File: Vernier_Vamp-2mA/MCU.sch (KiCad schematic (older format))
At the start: 11 parts

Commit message: 1.0C Initial commit
-Fixed amplifier output
-Changed connectors to IDC
-Via perimeter added
TODO:
Add shielding over analogue section
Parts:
- removed A1: Arduino_Nano_v3.x, Module:Arduino_Nano, symbol MCU_Module:Arduino_Nano_v3.x
- removed R50: 0R, Resistor_SMD:R_0603_1608Metric_Pad1.05x0.95mm_HandSolder, symbol Device:R_Small
- added A1: Arduino_Nano_Every, Module:Arduino_Nano, symbol MCU_Module:Arduino_Nano_Every
- added JP3, JP4: SolderJumper_2_Open, Jumper:SolderJumper-2_P1.3mm_Open_Pad1.0x1.5mm, symbol Jumper:SolderJumper_2_Open
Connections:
- net labels added: +5V
- no-connect marks 20 -> 19
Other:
- note added: "MPM3610 SMPS\n(Potentially noisy)"
- note added: "Schottky diode on the USB 5V rail.\nDon't bridge if Vin is used."
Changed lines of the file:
@@
 Comment4 ""
 $EndDescr
-$Comp
-L power:GNDD #PWR0196
-U 1 1 5E449396
-P 5900 5050
-AR Path="/5E1DEB8C/5E449396" Ref="#PWR0196"  Part="1"
-AR Path="/5E5EF2D7/5E449396" Ref="#PWR?"  Part="1"
-F 0 "#PWR0196" H 5900 4800 50  0001 C CNN
-F 1 "GNDD" H 5904 4895 50  0000 C CNN
-F 2 "" H 5900 5050 50  0001 C CNN
-F 3 "" H 5900 5050 50  0001 C CNN
-	1    5900 5050
-	1    0    0    -1
-$EndComp
-Wire Wire Line
-	5850 4800 5850 4900
-Wire Wire Line
-	5850 4900 5900 4900
-Wire Wire Line
-	5950 4900 5950 4800
-Wire Wire Line
-	5900 4900 5900 5050
-Connection ~ 5900 4900
-Wire Wire Line
-	5900 4900 5950 4900
 Text HLabel 4700 4500 0    50   Output ~ 0
 CLK
-Text HLabel 4700 4200 0    50   Output ~ 0
+Text HLabel 4700 4100 0    50   Output ~ 0
 ~CS
+Text HLabel 4700 4300 0    50   Output ~ 0
+SDI
+Text HLabel 4700 4400 0    50   Output ~ 0
+SDO
 Wire Wire Line
 	5350 4500 4700 4500
 Wire Wire Line
-	4700 4200 5350 4200
+	4700 4100 5350 4100
+Wire Wire Line
+	4700 4300 5350 4300
 Wire Wire Line
 	4700 4400 5350 4400
-Wire Wire Line
-	4700 4300 5350 4300
-NoConn ~ 5350 3700
-NoConn ~ 5350 3600
-NoConn ~ 5350 3500
-NoConn ~ 5350 3400
-NoConn ~ 6350 3600
-NoConn ~ 6350 3800
-NoConn ~ 6350 3900
-NoConn ~ 6350 4000
-NoConn ~ 6350 4100
-NoConn ~ 6350 4200
-NoConn ~ 6350 4300
-NoConn ~ 6350 4400
-NoConn ~ 6350 4500
-Text HLabel 4700 4100 0    50   Output ~ 0
+Text HLabel 4700 4000 0    50   Output ~ 0
 ~LDAC
-Text HLabel 4700 4000 0    50   Output ~ 0
+Text HLabel 4700 3900 0    50   Output ~ 0
 MSB
-NoConn ~ 5350 3800
-Wire Wire Line
-	4700 4000 5350 4000
-Wire Wire Line
-	5350 4100 4700 4100
+Wire Wire Line
+	4700 3900 5350 3900
+Wire Wire Line
+	5350 4000 4700 4000
 Text HLabel 4150 5900 2    50   Output ~ 0
 ~RS
-NoConn ~ 5350 3200
-NoConn ~ 5350 3300
-NoConn ~ 5950 2800
 $Comp
 L power:GNDD #PWR0205
@@
 	2350 6200 2350 6750
 $Comp
-L MCU_Module:Arduino_Nano_v3.x A1
-U 1 1 5E447129
-P 5850 3800
-AR Path="/5E1DEB8C/5E447129" Ref="A1"  Part="1"
-AR Path="/5E5EF2D7/5E447129" Ref="A?"  Part="1"
-F 0 "A1" H 6350 5050 50  0000 C CNN
-F 1 "Arduino_Nano_v3.x" H 6450 4950 50  0000 C CNN
-F 2 "Module:Arduino_Nano" H 5850 3800 50  0001 C CIN
-F 3 "http://www.mouser.com/pdfdocs/Gravitech_Arduino_Nano3_0.pdf" H 5850 3800 50  0001 C CNN
-	1    5850 3800
-	1    0    0    -1
-$EndComp
-$Comp
 L power:+5VD #PWR0117
 U 1 1 610CFB70
@@
 Text HLabel 4150 6500 2    50   Output ~ 0
 ~CS
+Text HLabel 4150 6350 2    50   Output ~ 0
+SDI
 Text HLabel 4150 6200 2    50   Output ~ 0
-SDI
+SDO
 Wire Wire Line
 	3500 6050 4150 6050
@@
 	4150 6500 3500 6500
 Wire Wire Line
+	4150 6350 3500 6350
+Wire Wire Line
 	4150 6200 3500 6200
-Wire Wire Line
-	4150 6350 3500 6350
 Text HLabel 4150 6650 2    50   Output ~ 0
 ~LDAC
@@
 Wire Wire Line
 	4150 5900 3500 5900
-Text HLabel 4700 3900 0    50   Output ~ 0
+Text HLabel 4700 3800 0    50   Output ~ 0
 ~RS
 Wire Wire Line
-	5350 3900 4700 3900
-NoConn ~ 6350 3200
-NoConn ~ 6350 3300
-NoConn ~ 8000 4750
-Wire Wire Line
-	6050 2550 6050 2800
+	5350 3800 4700 3800
+Wire Wire Line
+	6050 2550 6050 2650
 Wire Wire Line
 	5750 2650 5750 2800
 Wire Wire Line
 	4700 2650 4700 2550
-Wire Wire Line
-	4700 2650 5100 2650
-$Comp
-L Device:R_Small R?
-U 1 1 5EE38105
-P 5200 2650
-AR Path="/5E1DD6A9/5EE38105" Ref="R?"  Part="1"
-AR Path="/5E1DD6A9/5EC279B2/5EE38105" Ref="R?"  Part="1"
-AR Path="/5E1DEB8C/5EE38105" Ref="R50"  Part="1"
-F 0 "R50" V 5004 2650 50  0000 C CNN
-F 1 "0R" V 5095 2650 50  0000 C CNN
-F 2 "Resistor_SMD:R_0603_1608Metric_Pad1.05x0.95mm_HandSolder" H 5200 2650 50  0001 C CNN
-F 3 "~" H 5200 2650 50  0001 C CNN
-	1    5200 2650
-	0    1    1    0
-$EndComp
 $Comp
 L power:PWR_FLAG #FLG0107
@@
 Wire Wire Line
 	5450 2650 5750 2650
-Text HLabel 4150 6350 2    50   Output ~ 0
-SDO
 Text HLabel 4700 4400 0    50   Output ~ 0
 SDO
 Text HLabel 4700 4300 0    50   Output ~ 0
 SDI
+NoConn ~ 5350 3000
+NoConn ~ 5350 3100
+NoConn ~ 5350 3300
+NoConn ~ 5350 3400
+NoConn ~ 5350 3500
+NoConn ~ 5350 3600
+NoConn ~ 5350 3700
+NoConn ~ 6350 3600
+NoConn ~ 6350 3200
+NoConn ~ 6350 3300
+NoConn ~ 6350 3800
+NoConn ~ 6350 3900
+NoConn ~ 6350 4000
+NoConn ~ 6350 4100
+NoConn ~ 6350 4200
+NoConn ~ 6350 4300
+NoConn ~ 6350 4400
+NoConn ~ 6350 4500
+Wire Wire Line
+	5850 4800 5850 4950
+$Comp
+L power:GNDD #PWR0196
+U 1 1 5FA351DD
+P 5850 4950
+AR Path="/5E1DEB8C/5FA351DD" Ref="#PWR0196"  Part="1"
+AR Path="/5E5EF2D7/5FA351DD" Ref="#PWR?"  Part="1"
+F 0 "#PWR0196" H 5850 4700 50  0001 C CNN
+F 1 "GNDD" H 5854 4795 50  0000 C CNN
+F 2 "" H 5850 4950 50  0001 C CNN
+F 3 "" H 5850 4950 50  0001 C CNN
+	1    5850 4950
+	1    0    0    -1
+$EndComp
+$Comp
+L MCU_Module:Arduino_Nano_Every A1
+U 1 1 5FA2A758
+P 5850 3800
+F 0 "A1" H 5250 2850 50  0000 C CNN
+F 1 "Arduino_Nano_Every" H 5000 2750 50  0000 C CNN
+F 2 "Module:Arduino_Nano" H 5850 3800 50  0001 C CIN
+F 3 "https://content.arduino.cc/assets/NANOEveryV3.0_sch.pdf" H 5850 3800 50  0001 C CNN
+	1    5850 3800
+	1    0    0    -1
+$EndComp
+NoConn ~ 5950 2800
+$Comp
+L Jumper:SolderJumper_2_Open JP3
+U 1 1 5FB9E809
+P 5150 2650
+F 0 "JP3" H 5150 2763 50  0000 C CNN
+F 1 "SolderJumper_2_Open" H 5150 2764 50  0001 C CNN
+F 2 "Jumper:SolderJumper-2_P1.3mm_Open_Pad1.0x1.5mm" H 5150 2650 50  0001 C CNN
+F 3 "~" H 5150 2650 50  0001 C CNN
+	1    5150 2650
+	1    0    0    -1
+$EndComp
+Wire Wire Line
+	4700 2650 5000 2650
+$Comp
+L Jumper:SolderJumper_2_Open JP4
+U 1 1 5FBA0FCC
+P 6450 2650
+F 0 "JP4" H 6450 2763 50  0000 C CNN
+F 1 "SolderJumper_2_Open" H 6450 2764 50  0001 C CNN
+F 2 "Jumper:SolderJumper-2_P1.3mm_Open_Pad1.0x1.5mm" H 6450 2650 50  0001 C CNN
+F 3 "~" H 6450 2650 50  0001 C CNN
+	1    6450 2650
+	1    0    0    -1
+$EndComp
+$Comp
+L power:+5V #PWR?
+U 1 1 5FBA78FF
+P 6750 2550
+AR Path="/5E1DD6A9/5FBA78FF" Ref="#PWR?"  Part="1"
+AR Path="/5E1DEB8C/5FBA78FF" Ref="#PWR0212"  Part="1"
+F 0 "#PWR0212" H 6750 2400 50  0001 C CNN
+F 1 "+5V" H 6765 2723 50  0000 C CNN
+F 2 "" H 6750 2550 50  0001 C CNN
+F 3 "" H 6750 2550 50  0001 C CNN
+	1    6750 2550
+	1    0    0    -1
+$EndComp
+Wire Wire Line
+	6300 2650 6050 2650
+Connection ~ 6050 2650
+Wire Wire Line
+	6050 2650 6050 2800
+Wire Wire Line
+	6600 2650 6750 2650
+Wire Wire Line
+	6750 2650 6750 2550
+Text Notes 4500 2950 0    50   ~ 0
+MPM3610 SMPS\n(Potentially noisy)
+Wire Notes Line
+	5300 2500 5300 2750
+Wire Notes Line
+	5300 2750 5000 2750
+Wire Notes Line
+	5000 2750 5000 2500
+Wire Notes Line
+	5000 2500 5300 2500
+Text Notes 6450 2950 0    50   ~ 0
+Schottky diode on the USB 5V rail.\nDon't bridge if Vin is used.
+Wire Notes Line
+	6600 2750 6300 2750
+Wire Notes Line
+	6300 2750 6300 2500
+Wire Notes Line
+	6300 2500 6600 2500
+Wire Notes Line
+	6600 2500 6600 2750
 $EndSCHEMATC

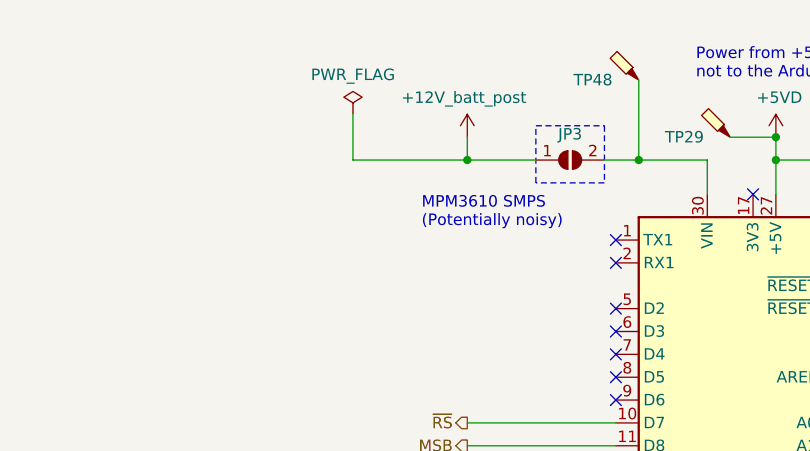
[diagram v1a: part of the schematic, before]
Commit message: Issue fixes
This commit, addresses following issues:
-Stray current at the output with only USB plugged in
-RFI Shield over analogue circuitry
-Wrong BNC connector footprint

Some general layout optimisation
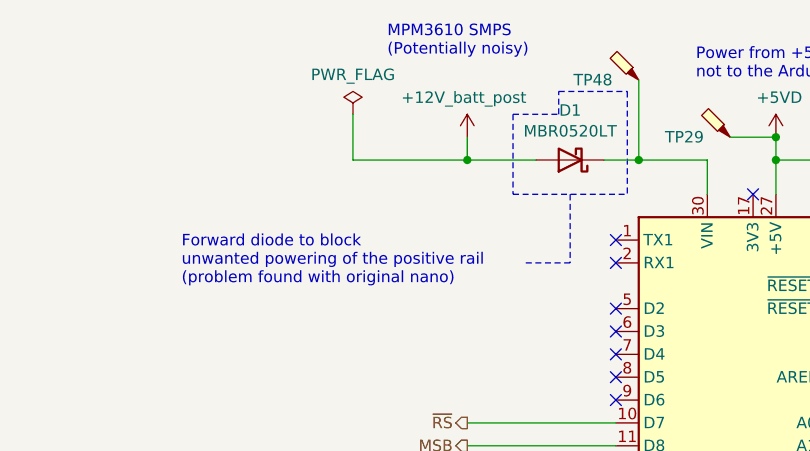
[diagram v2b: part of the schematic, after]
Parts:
- removed JP3: SolderJumper_2_Open, Jumper:SolderJumper-2_P1.3mm_Open_Pad1.0x1.5mm, symbol Jumper:SolderJumper_2_Open
- added D1: MBR0520LT, Diode_SMD:D_SOD-123, symbol Diode:MBR0520LT
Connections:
- net +12V_batt_post: now also D1.2 (A)
- net at A1.30 (VIN), TP48.1: now also D1.1 (K)
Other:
- note added: "Forward diode to block\nunwanted powering of the positive rail\n(problem found with original nano)"
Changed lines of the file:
@@
 $EndComp
 NoConn ~ 5950 2800
-$Comp
-L Jumper:SolderJumper_2_Open JP3
-U 1 1 5FB9E809
-P 5150 2650
-F 0 "JP3" H 5150 2763 50  0000 C CNN
-F 1 "SolderJumper_2_Open" H 5150 2764 50  0001 C CNN
-F 2 "Jumper:SolderJumper-2_P1.3mm_Open_Pad1.0x1.5mm" H 5150 2650 50  0001 C CNN
-F 3 "~" H 5150 2650 50  0001 C CNN
-	1    5150 2650
-	1    0    0    -1
-$EndComp
 Wire Wire Line
 	4700 2650 5000 2650
@@
 Wire Wire Line
 	6750 2650 6750 2550
-Text Notes 4500 2950 0    50   ~ 0
+Text Notes 4350 2200 0    50   ~ 0
 MPM3610 SMPS\n(Potentially noisy)
-Wire Notes Line
-	5300 2500 5300 2750
-Wire Notes Line
-	5300 2750 5000 2750
-Wire Notes Line
-	5000 2750 5000 2500
-Wire Notes Line
-	5000 2500 5300 2500
 Text Notes 6450 2950 0    50   ~ 0
 Schottky diode on the USB 5V rail.\nDon't bridge if Vin is used.
@@
 Wire Notes Line
 	6600 2500 6600 2750
+Wire Notes Line
+	4900 2450 5100 2450
+Wire Notes Line
+	5100 2450 5100 2350
+Wire Notes Line
+	5400 2350 5400 2800
+Wire Notes Line
+	4900 2450 4900 2800
+Wire Notes Line
+	5150 2800 5150 3100
+Wire Notes Line
+	5150 3100 4950 3100
+Text Notes 3450 3200 0    50   ~ 0
+Forward diode to block\nunwanted powering of the positive rail\n(problem found with original nano)
+$Comp
+L Diode:MBR0520LT D1
+U 1 1 5FC37ED8
+P 5150 2650
+F 0 "D1" H 5150 2433 50  0000 C CNN
+F 1 "MBR0520LT" H 5150 2524 50  0000 C CNN
+F 2 "Diode_SMD:D_SOD-123" H 5150 2475 50  0001 C CNN
+F 3 "http://www.onsemi.com/pub_link/Collateral/MBR0520LT1-D.PDF" H 5150 2650 50  0001 C CNN
+	1    5150 2650
+	-1   0    0    1
+$EndComp
+Wire Notes Line
+	5100 2350 5400 2350
+Wire Notes Line
+	4900 2800 5400 2800
 $EndSCHEMATC

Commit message: Change of J1 connector courtyard
PCB footprint change:
-J1 (1 mm pinheader) courtyard had been changed to pass DRC
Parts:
- A1: symbol MCU_Module:Arduino_Nano_Every -> Vernier_Vamp-2mA-rescue:Arduino_Nano_Every-MCU_Module
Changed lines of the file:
@@
 $EndComp
 $Comp
-L MCU_Module:Arduino_Nano_Every A1
+L Vernier_Vamp-2mA-rescue:Arduino_Nano_Every-MCU_Module A1
 U 1 1 5FA2A758
 P 5850 3800
+AR Path="/5FA2A758" Ref="A1"  Part="1"
+AR Path="/5E1DEB8C/5FA2A758" Ref="A1"  Part="1"
 F 0 "A1" H 5250 2850 50  0000 C CNN
 F 1 "Arduino_Nano_Every" H 5000 2750 50  0000 C CNN

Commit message: 1.0D Update
LCCD changes
-Addition of trigger for calibration
-PCB optimisation

HCCD changes
-New output stage designed
-Changes from 1.0C applied to HCCD
-New more optimised layout
-New shielding over analog section
-Addition of trigger for calibration

New symbols and footprint creation
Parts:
- removed JP4: SolderJumper_2_Open, Jumper:SolderJumper-2_P1.3mm_Open_Pad1.0x1.5mm, symbol Jumper:SolderJumper_2_Open
- added D2: MBR0520LT, Diode_SMD:D_SOD-123, symbol Diode:MBR0520LT
- added J9: Conn_01x02, Connector_PinHeader_2.54mm:PinHeader_1x02_P2.54mm_Vertical, symbol Connector_Generic:Conn_01x02
- A1: symbol Vernier_Vamp-2mA-rescue:Arduino_Nano_Every-MCU_Module -> Vernier_Vamp-2mA-rescue:Arduino_Nano_Every-MCU_Module-Vernier_Vamp-2mA-rescue
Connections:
- net +5V: now also D2.2 (A)
- net +5VD: now also D2.1 (K)
- net GNDD: now also J9.2 (Pin_2)
- net Trigger: now reaches A1.19 (A0)
- net Trigger: now also J9.1 (Pin_1)
- no-connect marks 19 -> 18
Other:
- note added: "Trigger output for calibration"
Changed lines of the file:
@@
 encoding utf-8
 Sheet 5 7
-Title "\"Vernier Vamp\" Coil Driver - 2mA"
-Date "2020-05-05"
-Rev "1.0B"
+Title "\"Vernier Vamp\" Coil Driver - LCCD"
+Date "2021-05-18"
+Rev "1.0D"
 Comp "Strathclyde University"
 Comment1 "Designed by: Marcin Mrozowski"
@@
 	4150 6500 3500 6500
 Wire Wire Line
+	4150 6200 3500 6200
+Wire Wire Line
 	4150 6350 3500 6350
-Wire Wire Line
-	4150 6200 3500 6200
 Text HLabel 4150 6650 2    50   Output ~ 0
 ~LDAC
@@
 NoConn ~ 6350 3200
 NoConn ~ 6350 3300
-NoConn ~ 6350 3800
 NoConn ~ 6350 3900
 NoConn ~ 6350 4000
@@
 $EndComp
 $Comp
-L Vernier_Vamp-2mA-rescue:Arduino_Nano_Every-MCU_Module A1
+L Vernier_Vamp-2mA-rescue:Arduino_Nano_Every-MCU_Module-Vernier_Vamp-2mA-rescue A1
 U 1 1 5FA2A758
 P 5850 3800
@@
 Wire Wire Line
 	4700 2650 5000 2650
-$Comp
-L Jumper:SolderJumper_2_Open JP4
-U 1 1 5FBA0FCC
-P 6450 2650
-F 0 "JP4" H 6450 2763 50  0000 C CNN
-F 1 "SolderJumper_2_Open" H 6450 2764 50  0001 C CNN
-F 2 "Jumper:SolderJumper-2_P1.3mm_Open_Pad1.0x1.5mm" H 6450 2650 50  0001 C CNN
-F 3 "~" H 6450 2650 50  0001 C CNN
-	1    6450 2650
-	1    0    0    -1
-$EndComp
 $Comp
 L power:+5V #PWR?
@@
 Wire Notes Line
 	4900 2800 5400 2800
+$Comp
+L Diode:MBR0520LT D2
+U 1 1 609E1E99
+P 6450 2650
+F 0 "D2" H 6450 2900 50  0000 C CNN
+F 1 "MBR0520LT" H 6450 2800 50  0000 C CNN
+F 2 "Diode_SMD:D_SOD-123" H 6450 2475 50  0001 C CNN
+F 3 "http://www.onsemi.com/pub_link/Collateral/MBR0520LT1-D.PDF" H 6450 2650 50  0001 C CNN
+	1    6450 2650
+	1    0    0    -1
+$EndComp
+$Comp
+L Connector_Generic:Conn_01x02 J9
+U 1 1 60A430EA
+P 1400 6100
+F 0 "J9" H 1480 6092 50  0000 L CNN
+F 1 "Conn_01x02" H 1480 6001 50  0000 L CNN
+F 2 "Connector_PinHeader_2.54mm:PinHeader_1x02_P2.54mm_Vertical" H 1400 6100 50  0001 C CNN
+F 3 "~" H 1400 6100 50  0001 C CNN
+	1    1400 6100
+	-1   0    0    -1
+$EndComp
+$Comp
+L power:GNDD #PWR0214
+U 1 1 60A4542E
+P 1600 6300
+AR Path="/5E1DEB8C/60A4542E" Ref="#PWR0214"  Part="1"
+AR Path="/5E5EF2D7/60A4542E" Ref="#PWR?"  Part="1"
+F 0 "#PWR0214" H 1600 6050 50  0001 C CNN
+F 1 "GNDD" H 1604 6145 50  0000 C CNN
+F 2 "" H 1600 6300 50  0001 C CNN
+F 3 "" H 1600 6300 50  0001 C CNN
+	1    1600 6300
+	1    0    0    -1
+$EndComp
+Wire Wire Line
+	1600 6200 1600 6300
+Wire Wire Line
+	6350 3800 7000 3800
+Text Label 7000 3800 0    50   ~ 0
+Trigger
+Text Label 1600 6100 0    50   ~ 0
+Trigger
+Wire Notes Line
+	750  5900 750  6650
+Wire Notes Line
+	750  6650 1950 6650
+Wire Notes Line
+	1950 6650 1950 5900
+Wire Notes Line
+	1950 5900 750  5900
+Text Notes 750  5800 0    50   ~ 0
+Trigger output for calibration
 $EndSCHEMATC
